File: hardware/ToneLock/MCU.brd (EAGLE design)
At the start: 55 x 50 mm, 46 parts, among them Q1 IRLML6346, U1 LD1117S33TR, U2 MP45DT02, U3 LIS3DSHTR, X3 MINI-USB-32005-201

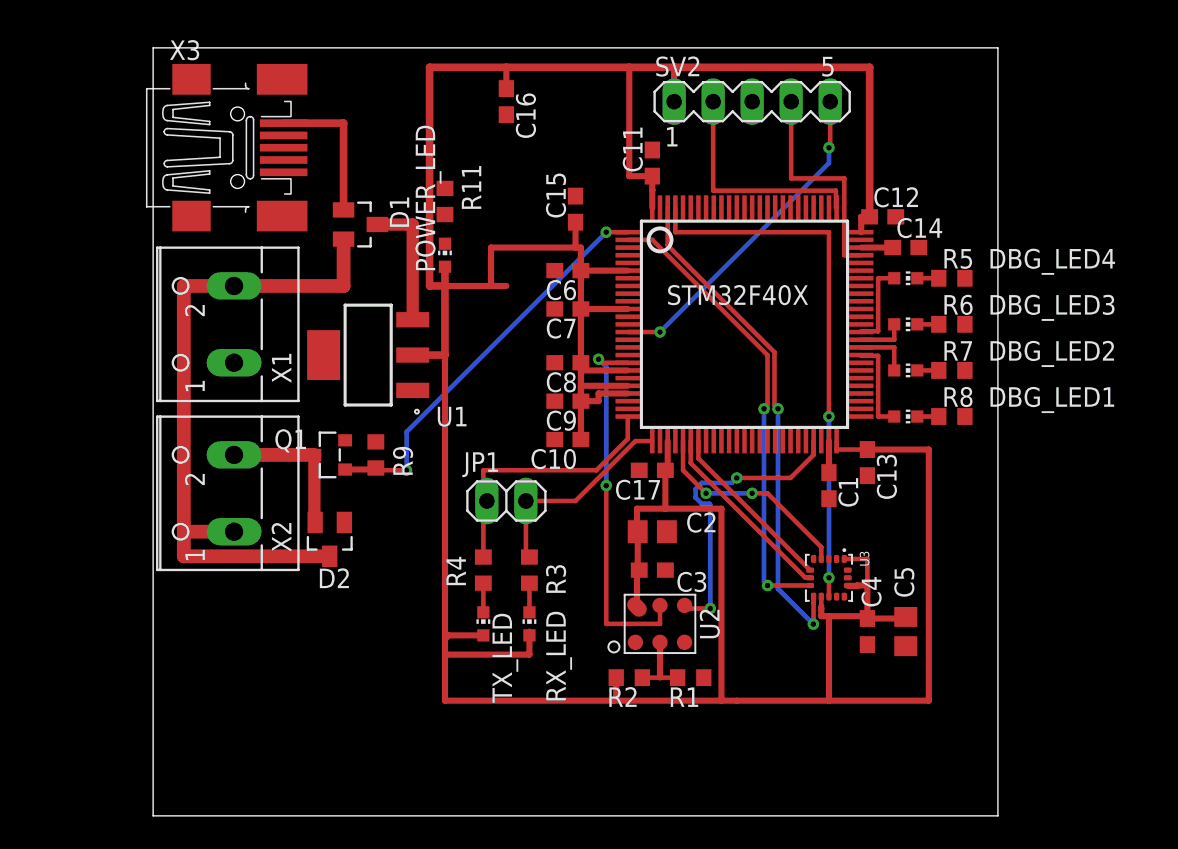
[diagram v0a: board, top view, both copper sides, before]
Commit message: Schematic ready for pour, rewired all supply lines
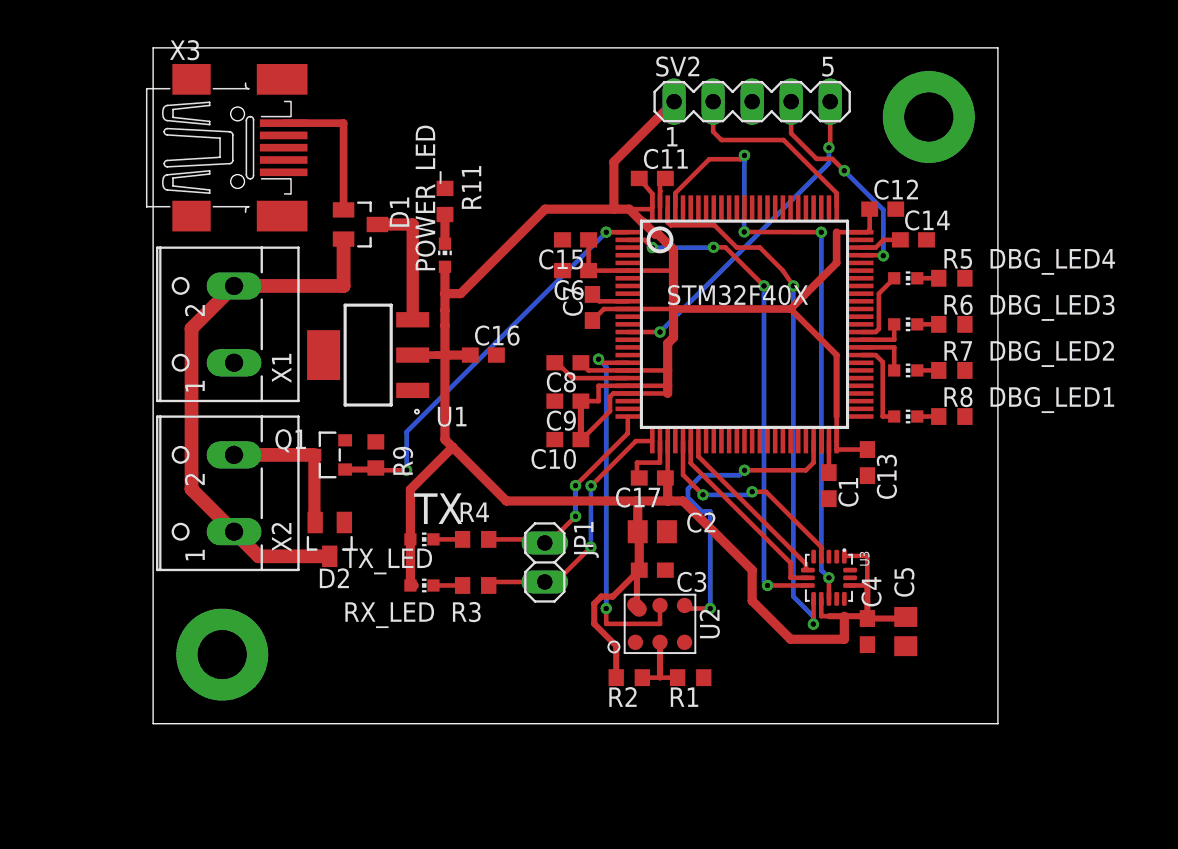
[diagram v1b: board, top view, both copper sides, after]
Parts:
- moved C16 16.6 mm to (29.0, 30.0), turned to 0 degrees
- moved RX_LED 7.43 mm to (25.0, 15.0), turned to 270 degrees
- moved TX_LED 6.80 mm to (25.0, 18.0), turned to 270 degrees
- moved JP1 4.72 mm to (33.0, 16.5), turned to 90 degrees
- moved R3 3.64 mm to (28.5, 15.0), turned to 0 degrees
- moved R4 2.06 mm to (28.5, 18.0), turned to 0 degrees
- moved C15 2.00 mm to (35.0, 37.5), turned to 180 degrees
- moved C7 1.60 mm to (36.1, 33.1), turned to 90 degrees
- moved C11 1.00 mm to (40.0, 41.5), turned to 0 degrees
- moved C14 0.71 mm to (57.0, 37.5)
- moved C12 0.50 mm to (55.0, 39.5)
- moved C17 0.50 mm to (40.0, 22.0)
- moved C6 0.50 mm to (35.0, 35.5)
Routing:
- net VDD: track 257.6 -> 204.9 mm
- net GND: track 0.00 -> 13.0 mm
- net +12V: track 43.8 -> 35.4 mm
- net MEMS_INT1: track 35.3 -> 40.5 mm, vias 2 -> 4
- net USART2_TX: track 17.7 -> 14.4 mm, vias 0 -> 2
- net USART2_RX: track 13.6 -> 16.9 mm, vias 0 -> 2
- net SWCLK: track 14.9 -> 12.6 mm
- net MEMS_INT2: track 32.8 -> 35.2 mm
- net MEMS_CS: track 30.3 -> 32.3 mm, vias 2 -> 4
- net N$1: track 0.00 -> 1.90 mm
- net MIC_CLK: track 19.7 -> 20.7 mm
- net N$2: track 2.05 -> 2.76 mm
- net DBG_LED4: track 5.65 -> 4.94 mm
- net SWDIO: vias 0 -> 2
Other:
- board size 55 x 50 mm -> 55 x 44 mm
- board text added: "TX"

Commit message: Routed, polygon poured, ready in theory
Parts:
- added TP1: TPB1,27, testpad:B1,27
- C15, C16: device resistor:C0603 -> resistor:C0805
- moved POWER_LED 2.92 mm to (29.0, 38.0)
- moved R11 2.92 mm to (29.0, 41.5)
- moved C16 2.24 mm to (27.0, 29.0), turned to 270 degrees
- moved C4 1.12 mm to (54.5, 11.0)
- moved C5 1.12 mm to (57.0, 11.0)
- moved DBG_LED1 0.71 mm to (57.0, 26.5)
- moved DBG_LED3 0.71 mm to (57.0, 32.5)
- moved R6 0.71 mm to (60.0, 32.5)
- moved R8 0.71 mm to (60.0, 26.5)
- moved DBG_LED2 0.50 mm to (57.0, 29.0)
- moved DBG_LED4 0.50 mm to (57.0, 35.0)
- moved R5 0.50 mm to (60.0, 35.0)
- moved R7 0.50 mm to (60.0, 29.0)
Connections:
- net MIC_PDM: now also TP1.TP
- net VDD: no longer U1.4
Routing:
- net VDD: track 204.9 -> 195.9 mm
- net GND: track 13.0 -> 4.73 mm, vias 0 -> 91
- net NRST: track 21.7 -> 27.0 mm, vias 2 -> 1
- net MEMS_INT1: track 40.5 -> 36.6 mm, vias 4 -> 2
- net MIC_PDM: track 24.1 -> 28.0 mm, vias 2 -> 3
- net MIC_CLK: track 20.7 -> 18.8 mm
- net +12V: track 35.4 -> 33.6 mm
- net MOSFET_GATE: track 26.4 -> 27.8 mm
- net N$6: track 8.50 -> 7.15 mm
- net +5V: track 9.55 -> 8.27 mm
- net MEMS_CS: track 32.3 -> 33.3 mm, vias 4 -> 2
- net DBG_LED1: track 5.88 -> 5.15 mm
- net MEMS_INT2: track 35.2 -> 34.6 mm
- net SWDIO: track 14.6 -> 14.0 mm
- net USART2_RX: vias 2 -> 1
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- added copper zone on layer 1, net GND
- added copper zone on layer 16, net GND
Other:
- board text added: "Rx"
- board text added: "Tx"
- board text removed: "TX"

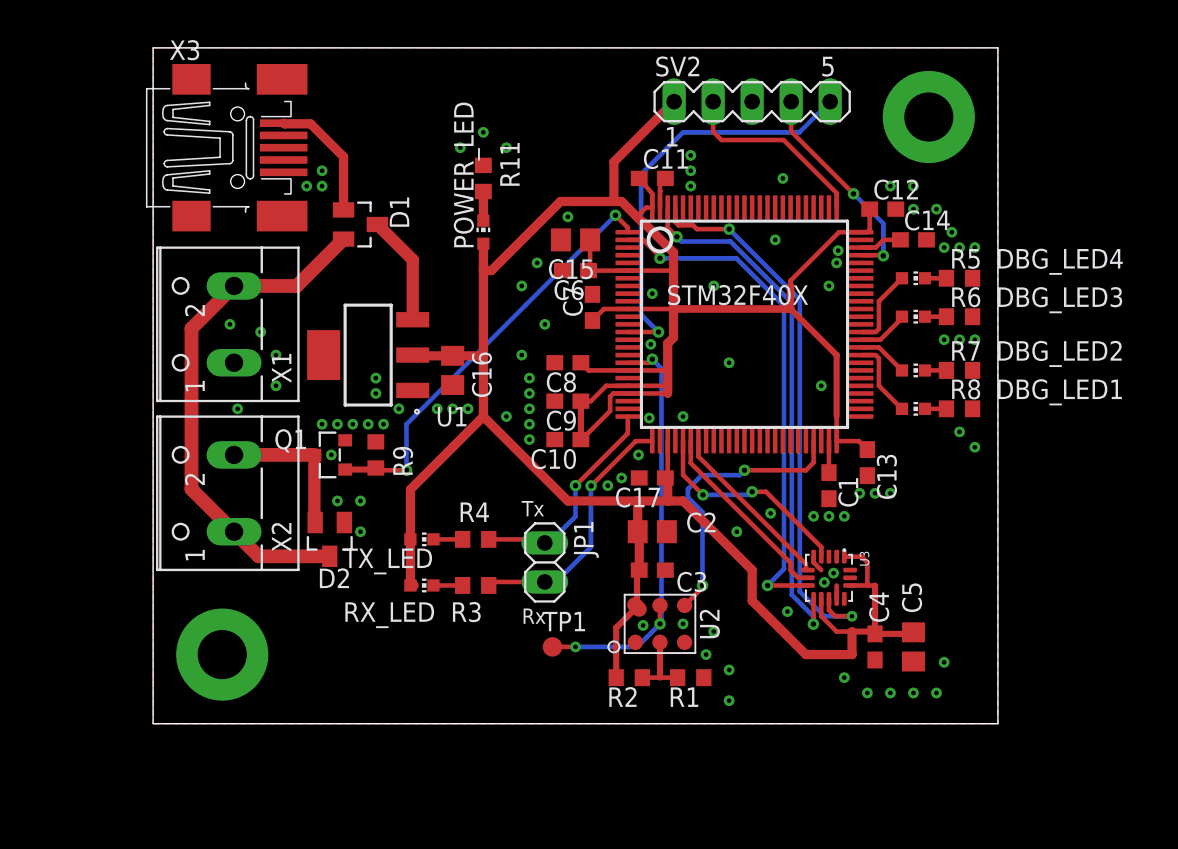
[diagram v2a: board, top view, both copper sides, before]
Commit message: Board now 50x44
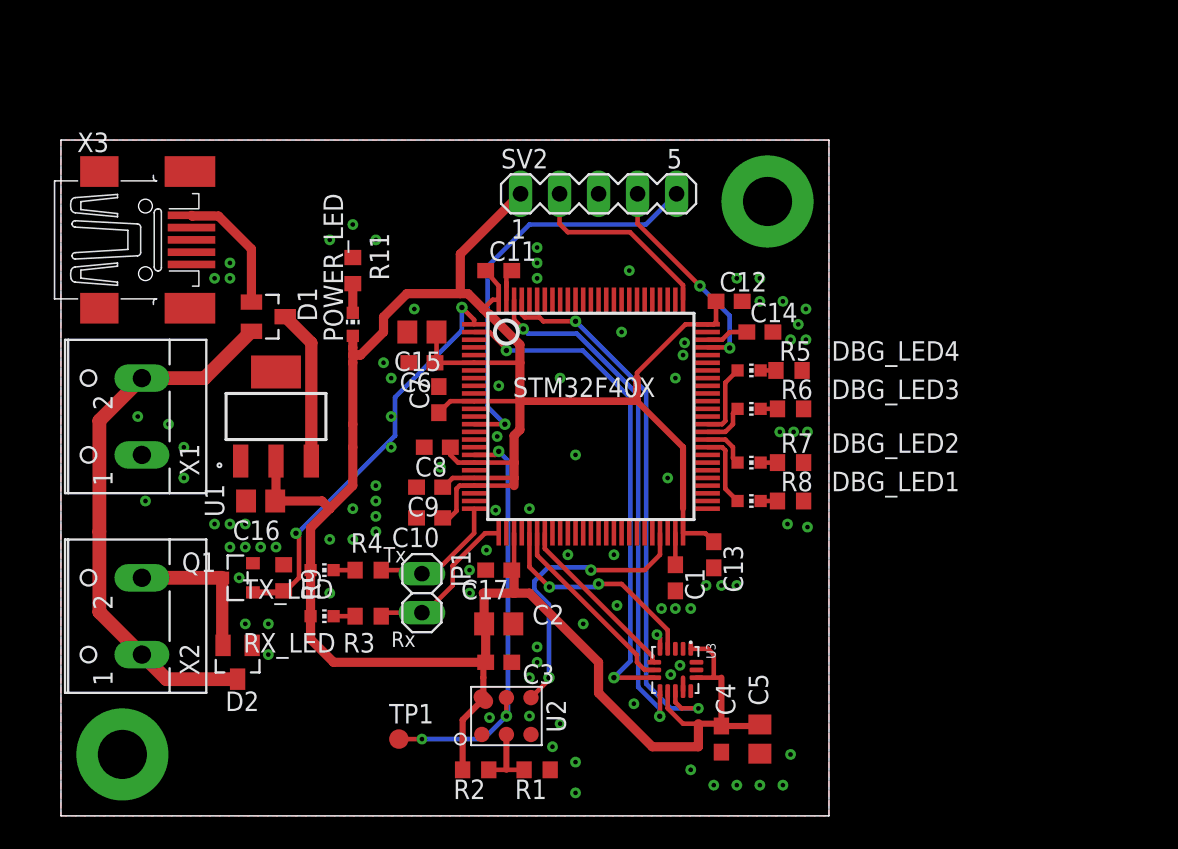
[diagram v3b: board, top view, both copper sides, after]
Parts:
- moved C16 15.1 mm to (14.5, 20.5), turned to 180 degrees
- moved R5 12.6 mm to (48.9, 29.0)
- moved R6 12.5 mm to (49.0, 26.5)
- moved R7 12.5 mm to (49.0, 23.0)
- moved R8 12.5 mm to (49.0, 20.5)
- moved DBG_LED1 12.3 mm to (46.3, 20.5)
- moved DBG_LED2 12.3 mm to (46.3, 23.0)
- moved DBG_LED3 12.3 mm to (46.3, 26.5)
- moved DBG_LED4 12.3 mm to (46.3, 29.0)
- moved C1 11.7 mm to (41.5, 15.5)
- moved C11 11.7 mm to (30.0, 35.5)
- moved C12 11.7 mm to (45.0, 33.5)
- moved C13 11.7 mm to (44.0, 17.0)
- moved C14 11.7 mm to (47.0, 31.5)
- moved C15 11.7 mm to (25.0, 31.5)
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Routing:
- net VDD: track 195.9 -> 186.1 mm
- net USART2_RX: track 16.9 -> 10.6 mm, vias 1 -> 0
- net USART2_TX: track 14.4 -> 8.83 mm, vias 1 -> 0
- net N$6: track 7.15 -> 10.1 mm
- net +12V: track 33.6 -> 35.6 mm
- net GND: track 4.73 -> 3.93 mm, vias 91 -> 96
- net MOSFET_GATE: track 27.8 -> 27.2 mm
- net N$7: track 1.90 -> 1.40 mm
- net N$4: track 1.90 -> 1.40 mm
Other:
- board size 55 x 44 mm -> 50 x 44 mm

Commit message: Ready for polygon
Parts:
- moved C4 8.38 mm to (36.8, 8.30)
- moved C5 8.38 mm to (39.3, 8.30)
- moved U3 4.72 mm to (37.5, 12.0), turned to 180 degrees
- moved POWER_LED 2.00 mm to (20.5, 34.0)
- moved R11 2.00 mm to (20.5, 37.5)
- moved C8 0.50 mm to (25.5, 24.0)
- moved C17 0.10 mm to (29.9, 16.0)
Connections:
- removed net MEMS_CS: U$1.2, U3.8
- new net MEMS_NCS: U$1.39, U3.8
- net MEMS_INT1: now also U$1.41; no longer U$1.97
- net MEMS_INT2: now also U$1.42; no longer U$1.98
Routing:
- net MEMS_CS: track 33.3 -> 0.00 mm, vias 2 -> 0
- net MEMS_INT1: track 36.6 -> 9.72 mm
- net MEMS_INT2: track 34.6 -> 7.95 mm
- net VDD: track 186.1 -> 172.5 mm
- net MIC_CLK: track 18.9 -> 26.9 mm, vias 2 -> 0
- net MEMS_NCS: track 0.00 -> 5.23 mm, vias 0 -> 2
- net MOSFET_GATE: track 27.2 -> 31.3 mm
- net MEMS_MISO: track 12.4 -> 8.56 mm
- net MEMS_SCK: track 14.3 -> 17.9 mm
- net MEMS_MOSI: track 11.4 -> 8.62 mm
- net GND: track 3.93 -> 2.05 mm, vias 96 -> 90
- net NRST: track 27.0 -> 26.4 mm, vias 1 -> 2

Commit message: Hardware ready to generate gerber
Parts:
- added TP2, TP3: TPB2,54, testpad:B2,54
- TP1: value TPB1,27 -> TPB2,54; device testpad:B1,27 -> testpad:B2,54
- moved C3 1.58 mm to (28.5, 10.5)
- moved R1 1.58 mm to (31.0, 2.50)
- moved R2 1.58 mm to (27.0, 2.50)
- moved C1 1.50 mm to (40.0, 15.5)
- moved C10 1.50 mm to (24.0, 19.4)
- moved C11 1.50 mm to (28.5, 35.5)
- moved C12 1.50 mm to (43.5, 33.5)
- moved C13 1.50 mm to (42.5, 17.0)
- moved C14 1.50 mm to (45.5, 31.5)
- moved C15 1.50 mm to (23.5, 31.5)
- moved C16 1.50 mm to (13.0, 20.5)
- moved C17 1.50 mm to (28.4, 16.0)
- moved C2 1.50 mm to (28.5, 12.5)
- moved C4 1.50 mm to (35.3, 8.30)
- moved C5 1.50 mm to (37.8, 8.30)
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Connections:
- net MEMS_SCK: now also TP3.TP
- net MIC_CLK: now also TP2.TP
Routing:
- net MEMS_SCK: track 17.9 -> 27.0 mm, vias 2 -> 4
- net MIC_CLK: track 26.9 -> 31.9 mm
- net NRST: track 26.4 -> 25.6 mm
- net MIC_PDM: track 28.0 -> 28.8 mm
- net VDD: track 172.5 -> 173.0 mm
- net GND: vias 90 -> 116
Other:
- board text added: "MEMS_CLK"
- board text added: "MIC_CLK"
- board text added: "MIC_PDM"
